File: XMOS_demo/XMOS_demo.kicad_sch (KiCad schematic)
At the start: 8 parts

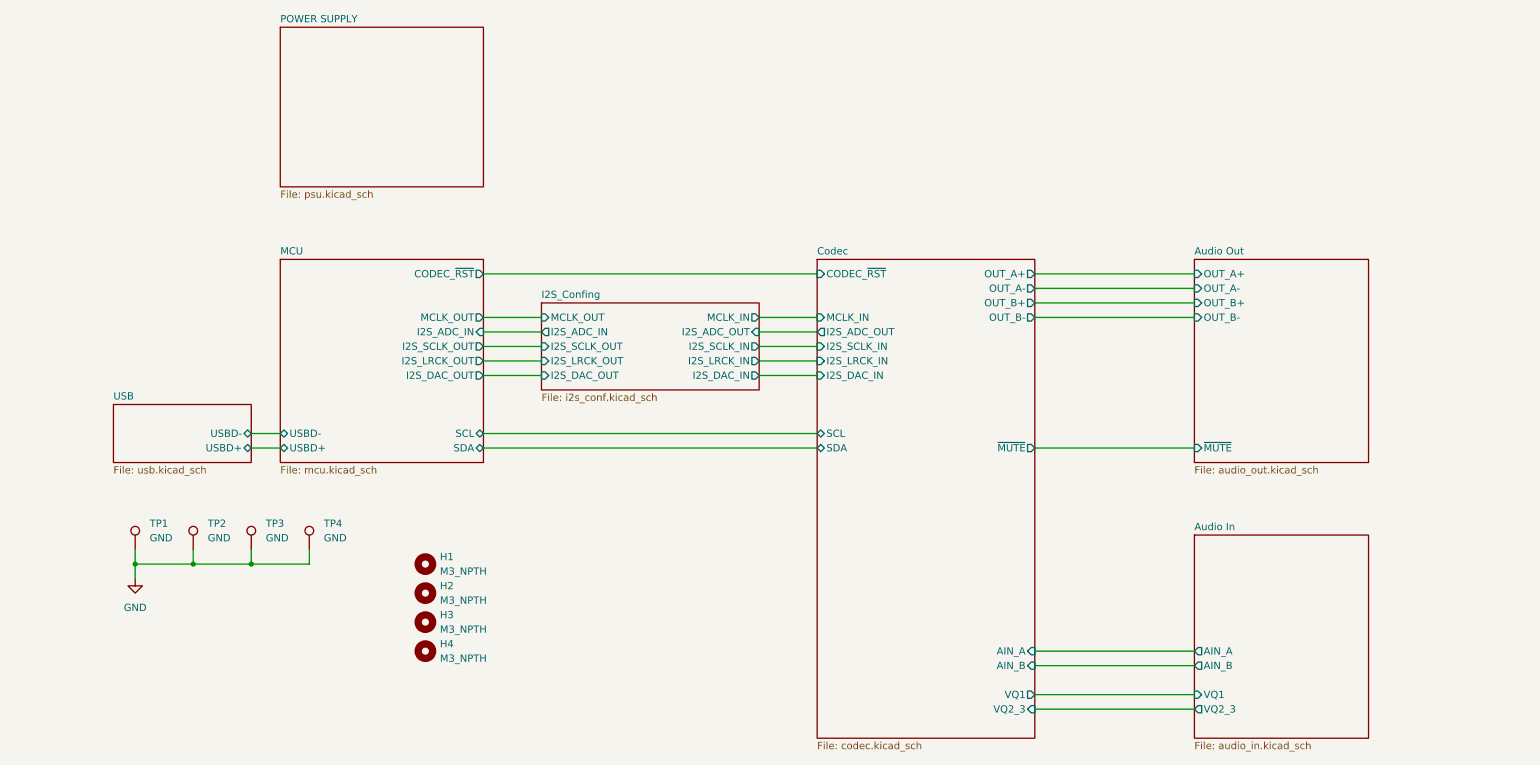
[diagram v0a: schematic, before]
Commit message: added schematic and simulation for active output filter
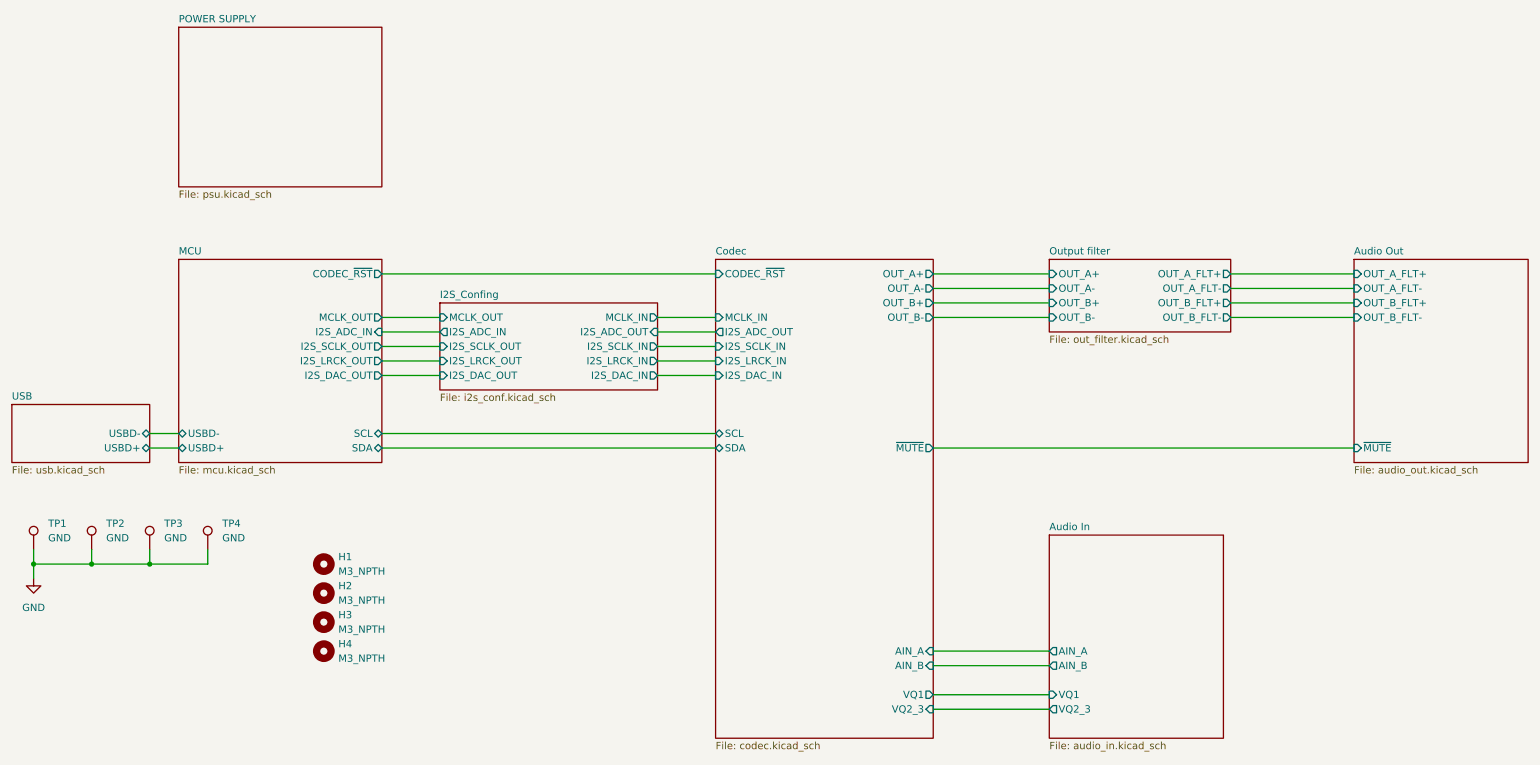
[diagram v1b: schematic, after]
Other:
- added sheet Output filter (out_filter.kicad_sch)
- sheet Audio Out ports: added OUT_A_FLT+, OUT_A_FLT-, OUT_B_FLT+, OUT_B_FLT-; removed OUT_A+, OUT_A-, OUT_B+, OUT_B-
- moved on the sheet: H1, H2, H3, H4, TP1, TP2, TP3, TP4

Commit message: Updated sch and pcb with active filter
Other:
- sheet Output filter ports: added ~{MUTE}; removed none
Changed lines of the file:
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@@
+	)
+	(junction
+		(at 187.96 109.22)
+		(diameter 0)
+		(color 0 0 0 0)
 	)
 	(junction
@@
 	(wire
 		(pts
+			(xy 187.96 109.22) (xy 248.92 109.22)
+		)
+		(stroke
+			(width 0)
+			(type default)
+		)
+	)
+	(wire
+		(pts
 			(xy 27.94 127) (xy 27.94 129.54)
 		)
@@
 	(wire
 		(pts
-			(xy 175.26 109.22) (xy 248.92 109.22)
+			(xy 175.26 109.22) (xy 187.96 109.22)
+		)
+		(stroke
+			(width 0)
+			(type default)
+		)
+	)
+	(wire
+		(pts
+			(xy 195.58 99.06) (xy 187.96 99.06)
 		)
 		(stroke
@@
 		(pts
 			(xy 175.26 86.36) (xy 195.58 86.36)
+		)
+		(stroke
+			(width 0)
+			(type default)
+		)
+	)
+	(wire
+		(pts
+			(xy 187.96 99.06) (xy 187.96 109.22)
 		)
 		(stroke
@@
 	(sheet
 		(at 195.58 76.2)
-		(size 31.75 12.7)
+		(size 31.75 25.4)
 		(exclude_from_sim no)
 		(in_bom yes)
@@
 		)
 		(property "Sheetfile" "out_filter.kicad_sch"
-			(at 195.58 89.4846 0)
+			(at 195.58 102.1846 0)
 			(effects
 				(font
@@
 			)
 		)
+		(pin "~{MUTE}" input
+			(at 195.58 99.06 180)
+			(effects
+				(font
+					(size 1.27 1.27)
+				)
+				(justify left)
+			)
+		)
